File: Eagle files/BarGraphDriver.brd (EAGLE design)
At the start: 100 x 80 mm, 22 parts, among them IC1 74HC595D, IC2 74HC595D

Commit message: Fixes
Removed outer footprint of board so that each board is now the correct
size instead of that of the default footprint.
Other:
- board size 100 x 80 mm -> 33 x 27.9 mm
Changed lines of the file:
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@@
 <board>
 <plain>
-<wire x1="0" y1="0" x2="100" y2="0" width="0" layer="20"/>
-<wire x1="100" y1="0" x2="100" y2="80" width="0" layer="20"/>
-<wire x1="100" y1="80" x2="0" y2="80" width="0" layer="20"/>
-<wire x1="0" y1="80" x2="0" y2="0" width="0" layer="20"/>
 <wire x1="15.24" y1="50.8" x2="15.24" y2="22.86" width="0.2032" layer="20"/>
 <wire x1="15.24" y1="22.86" x2="48.26" y2="22.86" width="0.2032" layer="20"/>

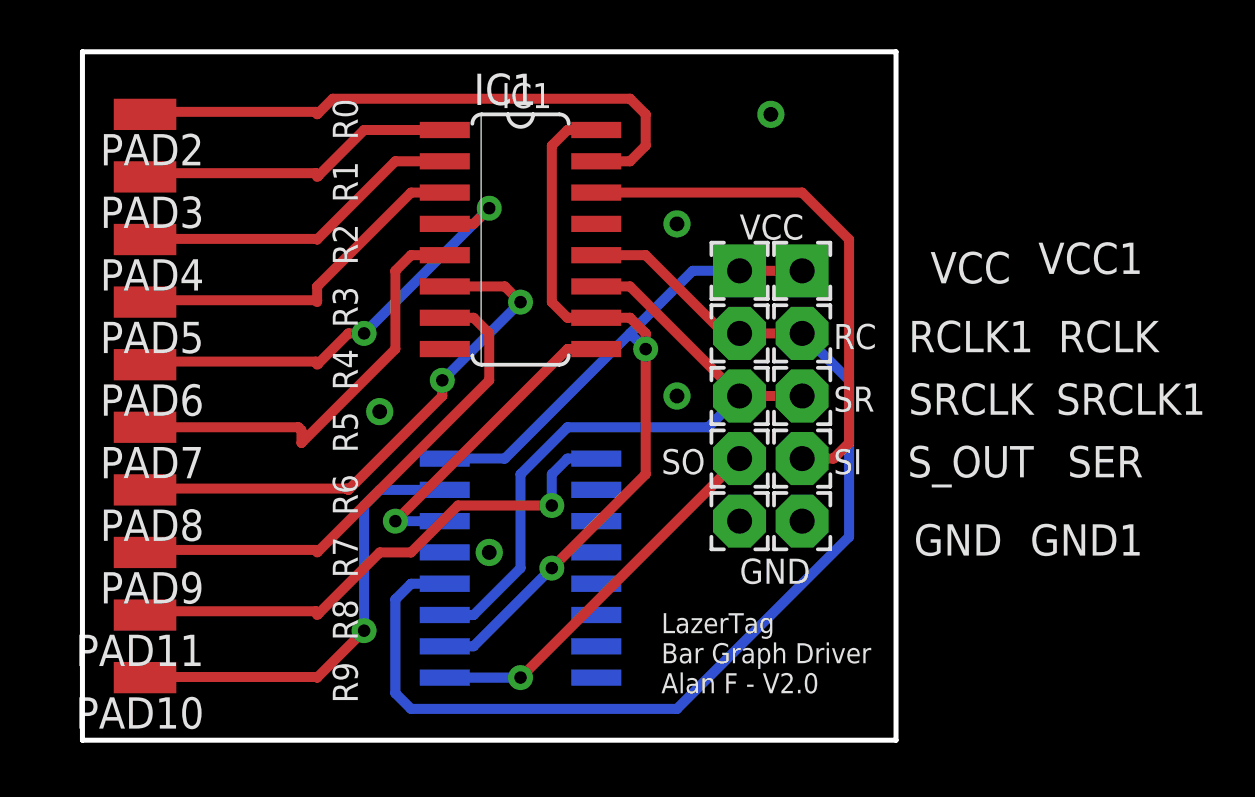
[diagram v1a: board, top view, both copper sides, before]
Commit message: aaaaaaaaaaaaaaaaaaaaaaaaaaaaaaaaaaaa
Cleaned up schematics, replaced wire solder points with header pin
mounts for standardization, recreated a broken file and dealt with the
confusion and insanity that followed.
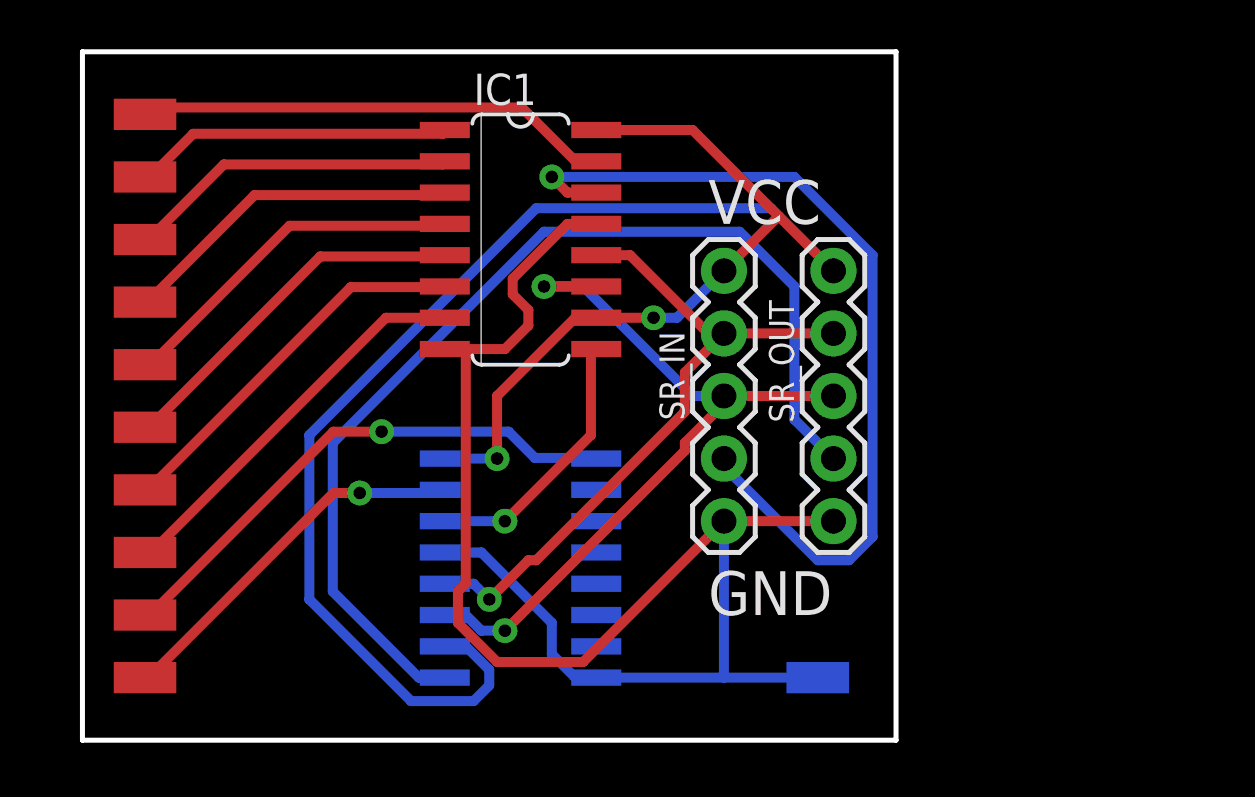
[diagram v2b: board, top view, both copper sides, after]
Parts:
- removed GND, GND1, RCLK, RCLK1, SER, SRCLK, SRCLK1, S_OUT: WIREPAD2,15/1,0, wirepad:2,15/1,0
- removed VCC, VCC1: WIREPAD2,15/1,0, smallWirepadSquare:2,15/1,0
- added PAD1: (no value), wirepad:SMD1,27-2,54
- added SR_IN, SR_OUT: (no value), SparkFun-Connectors:1X05
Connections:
- removed net SER: IC1.14, SER.1
- removed net SRCLK: IC1.11, IC2.11, SRCLK.1, SRCLK1.1
- removed net S_OUT: IC2.9, S_OUT.1
- new net SCLK: IC1.11, IC2.11, SR_IN.3, SR_OUT.3
- new net SER_IN: IC1.14, SR_IN.4
- new net SER_OUT: IC2.9, SR_OUT.4
- net GND: now also PAD1.1, SR_IN.5, SR_OUT.5; no longer GND.1, GND1.1
- net RCLK: now also SR_IN.2, SR_OUT.2; no longer RCLK.1, RCLK1.1
- net VCC: now also SR_IN.1, SR_OUT.1; no longer VCC.1, VCC1.1
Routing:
- net GND: track 0.00 -> 64.1 mm, vias 4 -> 0
- net SER_OUT: track 0.00 -> 42.9 mm
- net SER_IN: track 0.00 -> 36.2 mm, vias 0 -> 1
- net SCLK: track 0.00 -> 31.6 mm, vias 0 -> 2
- net SRCLK: track 28.1 -> 0.00 mm
- net VCC: track 48.1 -> 76.0 mm
- net SER: track 21.5 -> 0.00 mm
- net RCLK: track 46.4 -> 27.7 mm, vias 0 -> 1
- net S_OUT: track 15.6 -> 0.00 mm, vias 1 -> 0
- net N$17: track 22.2 -> 15.8 mm, vias 2 -> 0
- net N$11: track 24.5 -> 19.4 mm
- net N$18: track 21.0 -> 16.2 mm
- net N$15: track 18.9 -> 14.6 mm, vias 2 -> 0
- net N$19: track 18.3 -> 15.6 mm
- net N$16: track 17.7 -> 15.1 mm
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- removed copper zone on layer 1, net GND
- removed copper zone on layer 16, net GND
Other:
- board text added: "LazerTag Bar Graph Driver Alan F - V2.1 Greg T. (mod)"
- board text removed: "IC1"
- board text removed: "IC2"
- board text removed: "LazerTag Bar Graph Driver Alan F - V2.0"
- board text removed: "R0"
- board text removed: "R1"
- board text removed: "R2"
- board text removed: "R3"
- board text removed: "R4"
- board text removed: "R5"
- board text removed: "R6"
- board text removed: "R7"
- board text removed: "R8"
- board text removed: "R9"
- board text removed: "RC"
- board text removed: "SI"
- board text removed: "SO"
- board text removed: "SR"

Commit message: Fixes
more fixes >:|
should e ready for fabbing
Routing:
- added copper zone on layer 1, net GND
- added copper zone on layer 16, net GND
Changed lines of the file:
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@@
 <?xml version="1.0" encoding="utf-8"?>
 <!DOCTYPE eagle SYSTEM "eagle.dtd">
-<eagle version="7.5.0">
+<eagle version="7.4.0">
 <drawing>
 <settings>
@@
 <wire x1="41.275" y1="31.75" x2="35.56" y2="26.035" width="0.4064" layer="1"/>
 <wire x1="30.7975" y1="38.735" x2="29.9466" y2="38.735" width="0.4064" layer="1"/>
+<polygon width="0.4064" layer="16">
+<vertex x="15.24" y="50.8"/>
+<vertex x="48.26" y="50.8"/>
+<vertex x="48.26" y="22.86"/>
+<vertex x="15.24" y="22.86"/>
+</polygon>
+<polygon width="0.4064" layer="1">
+<vertex x="15.24" y="50.8"/>
+<vertex x="48.26" y="50.8"/>
+<vertex x="48.26" y="22.86"/>
+<vertex x="15.24" y="22.86"/>
+</polygon>
 </signal>
 <signal name="VCC" class="1">
